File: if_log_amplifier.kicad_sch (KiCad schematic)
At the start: 56 parts, among them J301 Conn_Coaxial, U301 AD603AQ, U302 L78L05_TO92, U303 LM317L_TO92, U304 AD8307AN, U305 CA3140

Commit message: catching up
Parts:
- renumbered J301 to J6
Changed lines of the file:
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@@
-    (stroke (width 0) (type default) (color 0 0 0 0))
-  )
-  (wire (pts (xy 314.96 78.74) (xy 318.77 78.74))
     (stroke (width 0) (type default) (color 0 0 0 0))
   )
@@
   (symbol (lib_id "Connector:Conn_Coaxial") (at 39.37 74.93 0) (mirror y) (unit 1)
     (in_bom yes) (on_board yes) (fields_autoplaced)
-    (property "Reference" "J301" (id 0) (at 39.6874 67.31 0))
+    (property "Reference" "J6" (id 0) (at 39.6874 67.31 0))
     (property "Value" "Conn_Coaxial" (id 1) (at 39.6874 69.85 0))
     (property "Footprint" "" (id 2) (at 39.37 74.93 0)

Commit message: test deletion
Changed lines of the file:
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@@
     (title "Spectrum Analyzer: IF and Log Amplifier")
     (date "2022-05-30")
-    (rev "0.1")
+    (rev "0.3")
     (company "Andy McCann KA3KAF and Doug McCann KA3KAG")
-    (comment 1 "Terry White K7TAU")
-    (comment 2 "Wes Hayward W7ZOI")
-    (comment 3 "Original Design By:")
+    (comment 2 "Terry White K7TAU")
+    (comment 3 "Wes Hayward W7ZOI")
+    (comment 4 "Original Design By:")
   )
   (junction (at 322.58 78.74) (diameter 0) (color 0 0 0 0)
@@
       (effects (font (size 1.27 1.27)) (justify left) hide)
     )
-  )
-  (global_label "Out" (shape output) (at 318.77 78.74 0) (fields_autoplaced)
-    (effects (font (size 1.27 1.27)) (justify left))
-    (property "Intersheet References" "${INTERSHEET_REFS}" (id 0) (at 324.3883 78.6606 0)
-      (effects (font (size 1.27 1.27)) (justify left) hide)
-    )

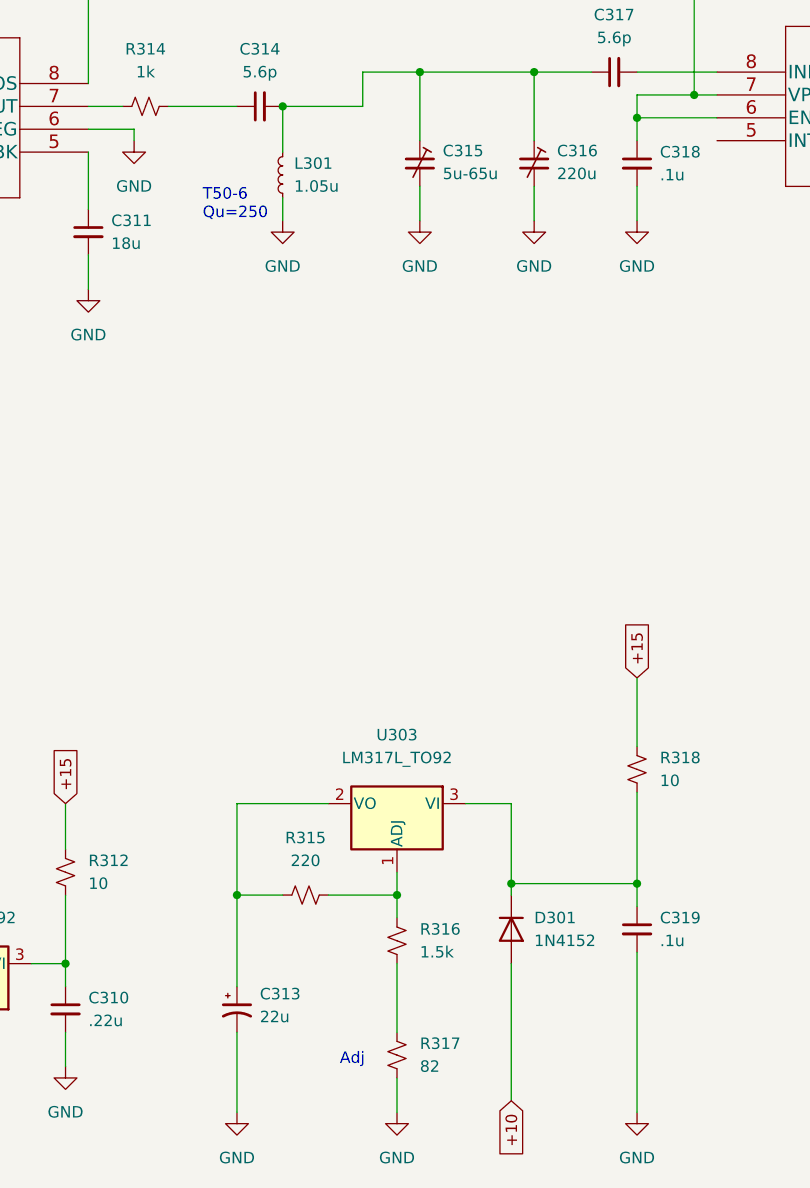
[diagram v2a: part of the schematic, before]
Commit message: corrected 10V power supply and component values in IF filter
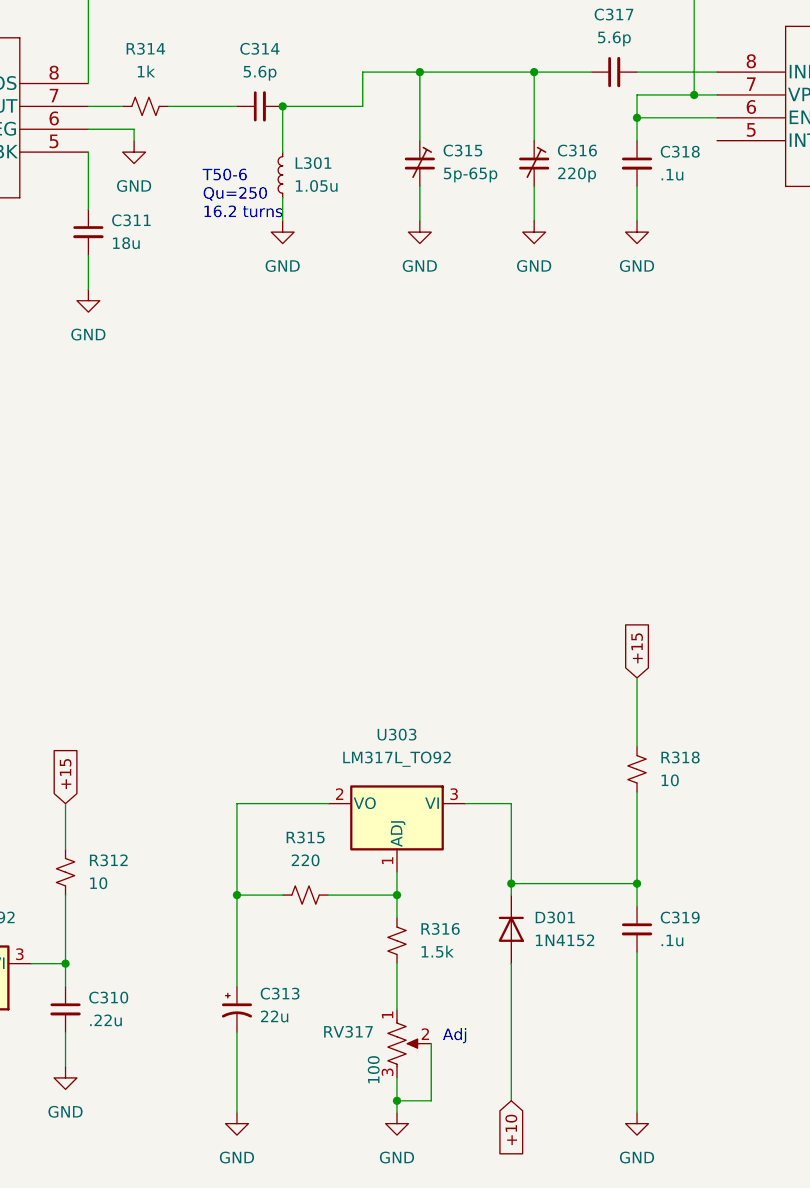
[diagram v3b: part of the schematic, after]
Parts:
- removed R317: 82, symbol Device:R_Small_US
- added RV317: 100, symbol Device:R_Potentiometer_US
- C315: value 5u-65u -> 5p-65p
- C316: value 220u -> 220p
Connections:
- net GND: now also RV317.2, RV317.3
- net at R316.2: now also RV317.1
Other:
- note added: "T50-6 Qu=250 16.2 turns"
- note removed: "T50-6 Qu=250"
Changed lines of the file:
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@@
   (junction (at 167.64 68.58) (diameter 0) (color 0 0 0 0)
   )
+  (junction (at 165.1 182.88) (diameter 0) (color 0 0 0 0)
+  )
   (junction (at 102.87 101.6) (diameter 0) (color 0 0 0 0)
   )
@@
   (junction (at 76.2 81.28) (diameter 0) (color 0 0 0 0)
   )
+  (wire (pts (xy 168.91 182.88) (xy 165.1 182.88))
+    (stroke (width 0) (type default) (color 0 0 0 0))
+  )
   (wire (pts (xy 280.67 91.44) (xy 274.32 91.44))
     (stroke (width 0) (type default) (color 0 0 0 0))
@@
     (stroke (width 0) (type default) (color 0 0 0 0))
   )
-  (wire (pts (xy 165.1 175.26) (xy 165.1 167.64))
-    (stroke (width 0) (type default) (color 0 0 0 0))
-  )
   (wire (pts (xy 157.48 160.02) (xy 165.1 160.02))
     (stroke (width 0) (type default) (color 0 0 0 0))
@@
     (stroke (width 0) (type default) (color 0 0 0 0))
   )
+  (wire (pts (xy 165.1 182.88) (xy 165.1 180.34))
+    (stroke (width 0) (type default) (color 0 0 0 0))
+  )
   (wire (pts (xy 50.8 77.47) (xy 50.8 74.93))
     (stroke (width 0) (type default) (color 0 0 0 0))
@@
     (stroke (width 0) (type default) (color 0 0 0 0))
   )
+  (wire (pts (xy 165.1 167.64) (xy 165.1 172.72))
+    (stroke (width 0) (type default) (color 0 0 0 0))
+  )
   (wire (pts (xy 198.12 52.07) (xy 198.12 40.64))
     (stroke (width 0) (type default) (color 0 0 0 0))
@@
     (stroke (width 0) (type default) (color 0 0 0 0))
   )
+  (wire (pts (xy 168.91 176.53) (xy 168.91 182.88))
+    (stroke (width 0) (type default) (color 0 0 0 0))
+  )
   (wire (pts (xy 76.2 81.28) (xy 76.2 109.22))
     (stroke (width 0) (type default) (color 0 0 0 0))
@@
     (stroke (width 0) (type default) (color 0 0 0 0))
   )
-  (wire (pts (xy 165.1 184.15) (xy 165.1 180.34))
+  (wire (pts (xy 165.1 184.15) (xy 165.1 182.88))
     (stroke (width 0) (type default) (color 0 0 0 0))
   )
@@
     (stroke (width 0) (type default) (color 0 0 0 0))
   )
-  (text "Adj" (at 158.75 179.07 0)
+  (text "Adj" (at 170.18 176.53 0)
     (effects (font (size 1.27 1.27)) (justify left bottom))
   )
-  (text "T50-6\nQu=250" (at 143.51 85.09 0)
+  (text "T50-6\nQu=250\n16.2 turns" (at 143.51 85.09 0)
     (effects (font (size 1.27 1.27)) (justify left bottom))
   )
@@
     (pin "1")
   )
-  (symbol (lib_id "Device:R_Small_US") (at 165.1 177.8 0) (unit 1)
-    (in_bom yes) (on_board yes) (fields_autoplaced)
-    (property "Reference" "R317" (id 0) (at 167.64 176.5299 0)
-      (effects (font (size 1.27 1.27)) (justify left))
-    )
-    (property "Value" "82" (id 1) (at 167.64 179.0699 0)
-      (effects (font (size 1.27 1.27)) (justify left))
-    )
-    (property "Footprint" "" (id 2) (at 165.1 177.8 0)
-      (effects (font (size 1.27 1.27)) hide)
-    )
-    (property "Datasheet" "~" (id 3) (at 165.1 177.8 0)
-      (effects (font (size 1.27 1.27)) hide)
-    )
-    (pin "1")
-    (pin "2")
+  (symbol (lib_id "Device:R_Potentiometer_US") (at 165.1 176.53 0) (unit 1)
+    (in_bom yes) (on_board yes)
+    (property "Reference" "RV317" (id 0) (at 162.56 175.2599 0)
+      (effects (font (size 1.27 1.27)) (justify right))
+    )
+    (property "Value" "100" (id 1) (at 162.56 177.7999 90)
+      (effects (font (size 1.27 1.27)) (justify right))
+    )
+    (property "Footprint" "" (id 2) (at 165.1 176.53 0)
+      (effects (font (size 1.27 1.27)) hide)
+    )
+    (property "Datasheet" "~" (id 3) (at 165.1 176.53 0)
+      (effects (font (size 1.27 1.27)) hide)
+    )
+    (pin "1")
+    (pin "2")
+    (pin "3")
   )
   (symbol (lib_id "Device:L_Small") (at 152.4 80.01 180) (unit 1)
@@
       (effects (font (size 1.27 1.27)) (justify left))
     )
-    (property "Value" "5u-65u" (id 1) (at 170.18 79.8829 0)
+    (property "Value" "5p-65p" (id 1) (at 170.18 79.8829 0)
       (effects (font (size 1.27 1.27)) (justify left))
     )
@@
       (effects (font (size 1.27 1.27)) (justify left))
     )
-    (property "Value" "220u" (id 1) (at 182.88 79.8829 0)
-      (effects (font (size 1.27 1.27)) (justify left))
-    )
+    (property "Value" "220p" (id 1) (at 182.88 79.8829 0)
+      (effects (font (size 1.27 1.27)) (justify left))
+    )

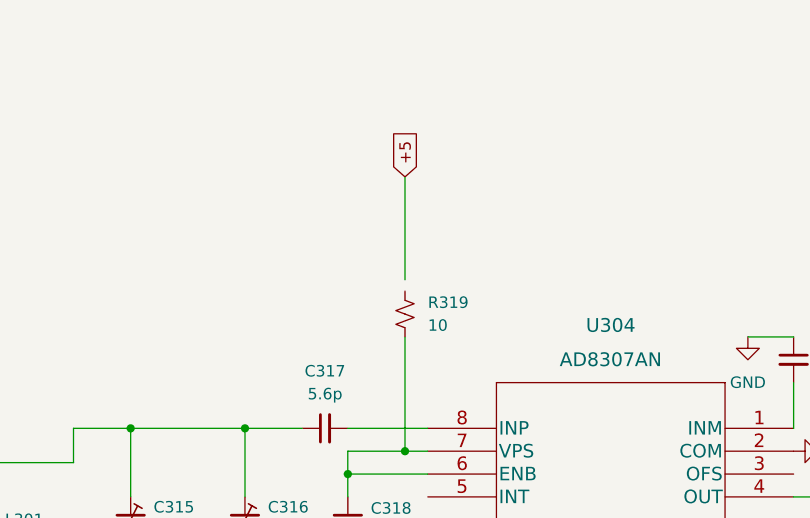
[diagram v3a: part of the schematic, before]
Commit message: fixed broken wire by R319
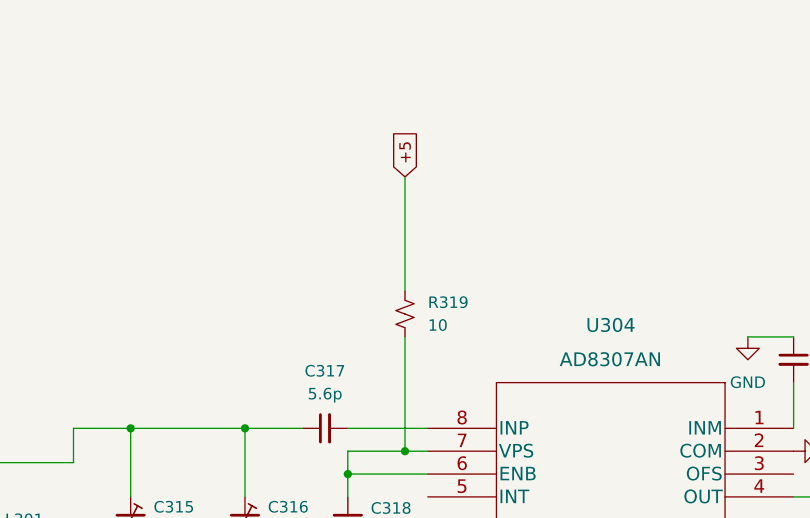
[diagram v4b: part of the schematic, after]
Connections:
- net +5: now also R319.1
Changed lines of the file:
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@@
     (stroke (width 0) (type default) (color 0 0 0 0))
   )
-  (wire (pts (xy 198.12 52.07) (xy 198.12 40.64))
+  (wire (pts (xy 198.12 40.64) (xy 198.12 53.34))
     (stroke (width 0) (type default) (color 0 0 0 0))
   )

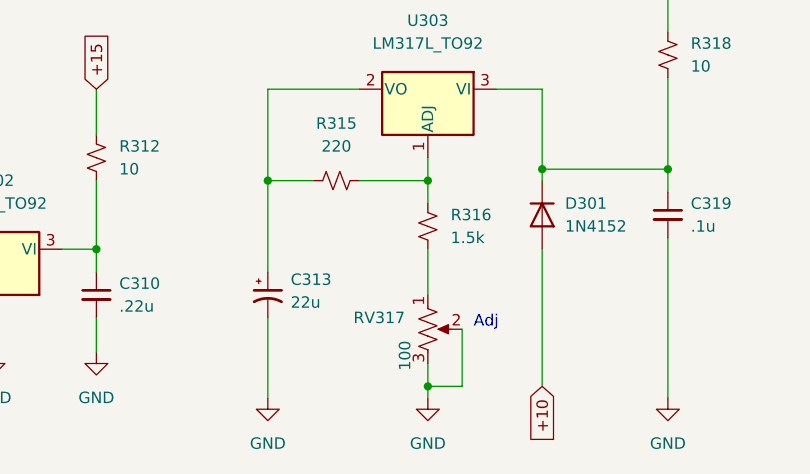
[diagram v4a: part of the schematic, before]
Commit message: added missing wire in 10V regulator
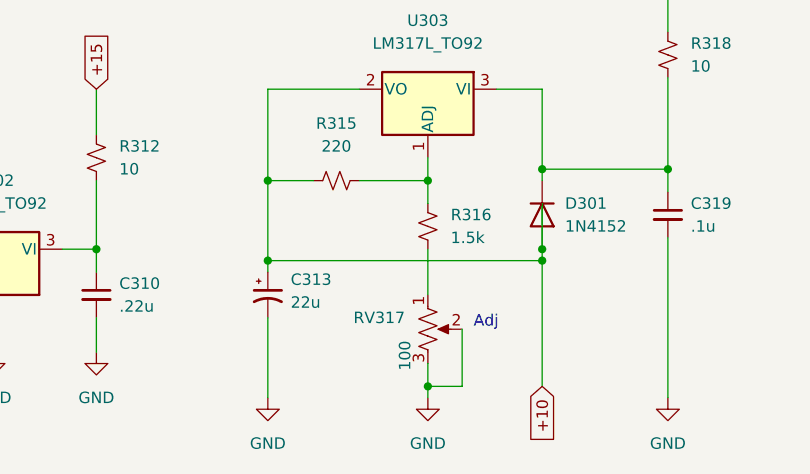
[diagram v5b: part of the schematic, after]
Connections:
- net +10: now also C313.1, R315.1, U303.2 (VO)
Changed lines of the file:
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@@
   (junction (at 245.11 76.2) (diameter 0) (color 0 0 0 0)
   )
+  (junction (at 177.8 167.64) (diameter 0) (color 0 0 0 0)
+  )
   (junction (at 59.69 173.99) (diameter 0) (color 0 0 0 0)
   )
+  (junction (at 177.8 168.91) (diameter 0) (color 0 0 0 0)
+  )
   (junction (at 191.77 158.75) (diameter 0) (color 0 0 0 0)
   )
@@
   (junction (at 102.87 101.6) (diameter 0) (color 0 0 0 0)
   )
+  (junction (at 147.32 168.91) (diameter 0) (color 0 0 0 0)
+  )
   (junction (at 48.26 46.99) (diameter 0) (color 0 0 0 0)
   )
@@
     (stroke (width 0) (type default) (color 0 0 0 0))
   )
-  (wire (pts (xy 177.8 167.64) (xy 177.8 182.88))
+  (wire (pts (xy 177.8 162.56) (xy 177.8 167.64))
     (stroke (width 0) (type default) (color 0 0 0 0))
   )
@@
     (stroke (width 0) (type default) (color 0 0 0 0))
   )
+  (wire (pts (xy 177.8 167.64) (xy 177.8 168.91))
+    (stroke (width 0) (type default) (color 0 0 0 0))
+  )
   (wire (pts (xy 36.83 156.21) (xy 36.83 173.99))
     (stroke (width 0) (type default) (color 0 0 0 0))
@@
     (stroke (width 0) (type default) (color 0 0 0 0))
   )
+  (wire (pts (xy 147.32 168.91) (xy 177.8 168.91))
+    (stroke (width 0) (type default) (color 0 0 0 0))
+  )
   (wire (pts (xy 50.8 74.93) (xy 44.45 74.93))
     (stroke (width 0) (type default) (color 0 0 0 0))
@@
     (stroke (width 0) (type default) (color 0 0 0 0))
   )
+  (wire (pts (xy 177.8 168.91) (xy 177.8 182.88))
+    (stroke (width 0) (type default) (color 0 0 0 0))
+  )
   (wire (pts (xy 93.98 167.64) (xy 101.6 167.64))
     (stroke (width 0) (type default) (color 0 0 0 0))
@@
     (stroke (width 0) (type default) (color 0 0 0 0))
   )
-  (wire (pts (xy 147.32 160.02) (xy 147.32 170.18))
+  (wire (pts (xy 147.32 160.02) (xy 147.32 168.91))
     (stroke (width 0) (type default) (color 0 0 0 0))
   )
@@
     (stroke (width 0) (type default) (color 0 0 0 0))
   )
+  (wire (pts (xy 147.32 168.91) (xy 147.32 170.18))
+    (stroke (width 0) (type default) (color 0 0 0 0))
+  )
